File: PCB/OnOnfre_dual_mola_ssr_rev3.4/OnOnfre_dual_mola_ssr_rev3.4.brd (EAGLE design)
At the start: 44.4 x 47.7 mm, 24 parts, among them J3Y S8050, J7 8p, K1 OMRON-G3MB-202P-SSR2, K2 OMRON-G3MB-202P-SSR2, U2 esp12

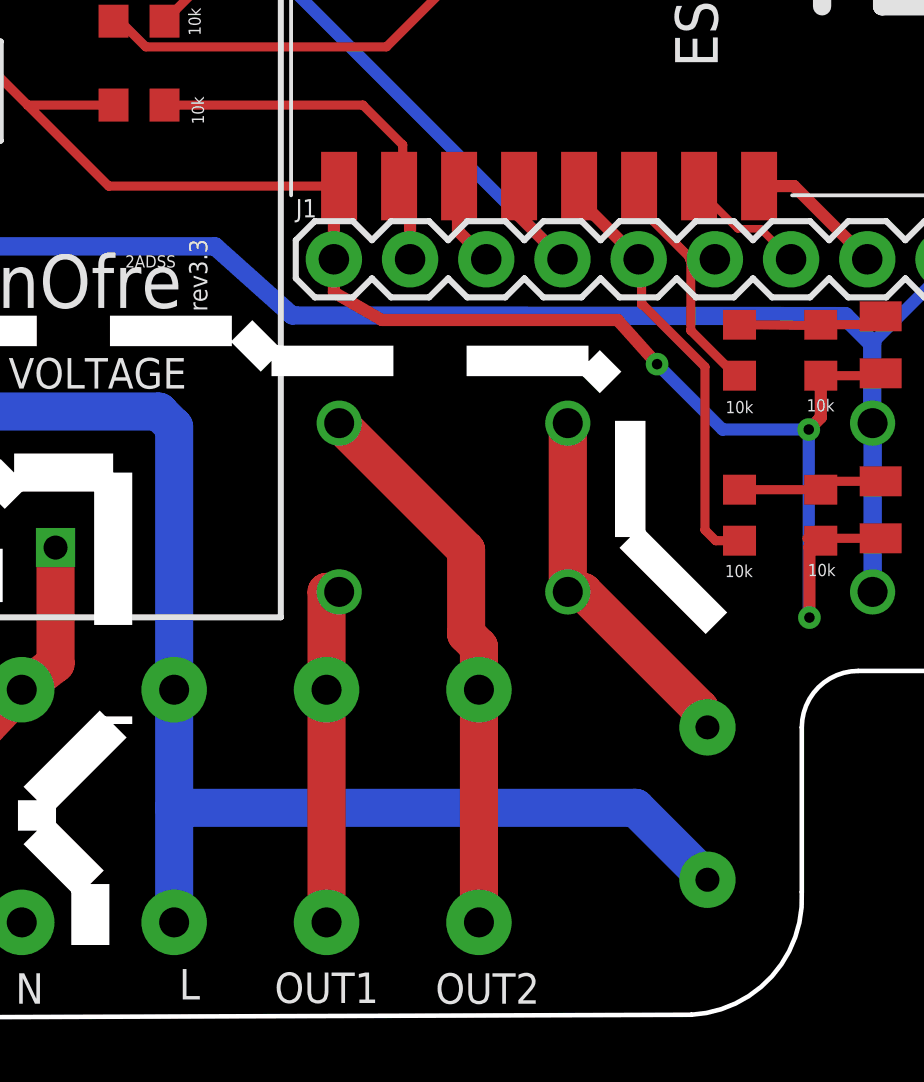
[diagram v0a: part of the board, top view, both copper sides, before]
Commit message: Rev 3.4, alteração de labels e numero de pinos
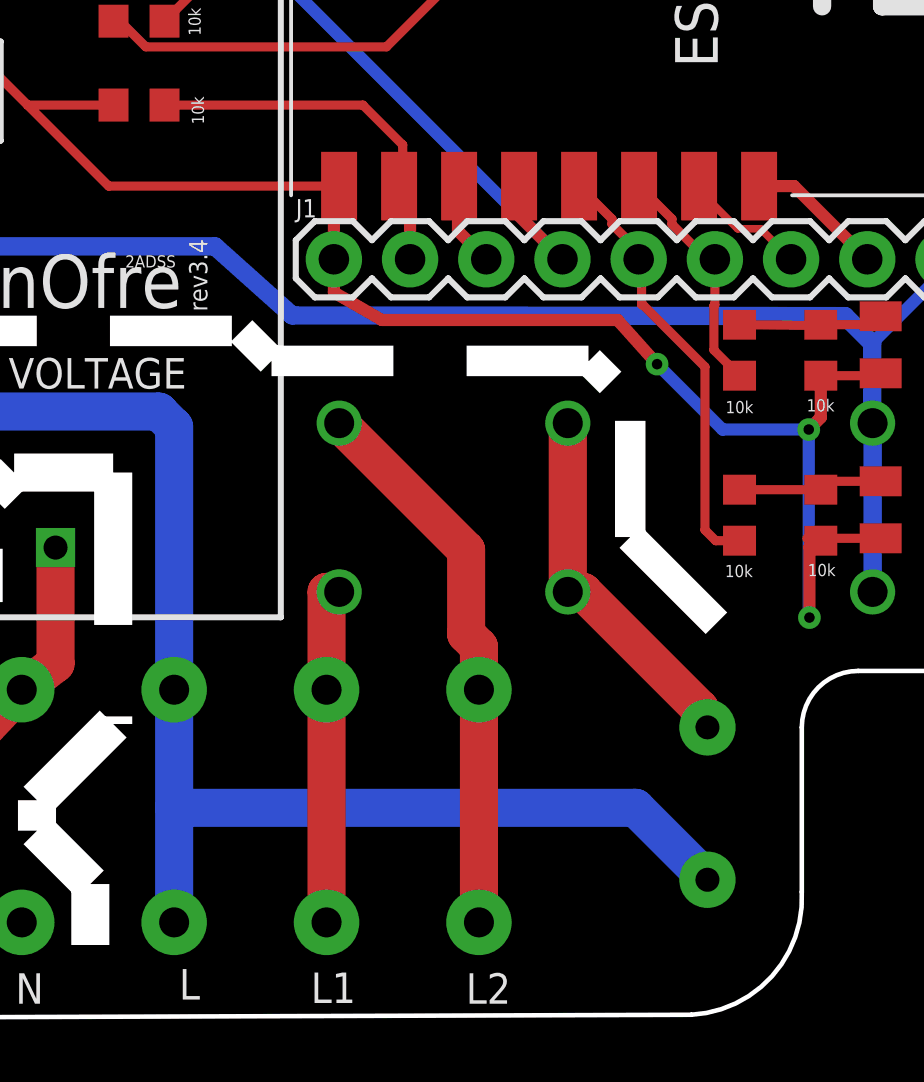
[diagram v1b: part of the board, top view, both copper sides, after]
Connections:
- net GPIO04: now also J1.5, R4.1; no longer J1.6, R1.1
- net GPIO05: now also J1.6, R1.1; no longer J1.5, R4.1
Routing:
- net GPIO05: track 14.6 -> 7.89 mm
- net GPIO04: track 8.65 -> 14.7 mm
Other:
- board text added: "L1"
- board text added: "L2"
- board text added: "rev3.4"
- board text removed: "OUT1"
- board text removed: "OUT2"
- board text removed: "rev3.3"
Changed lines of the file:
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@@
 <text x="27.8430875" y="27.2" size="1.016" layer="26" font="vector" ratio="13" rot="SMR270">02</text>
 <text x="30.39693125" y="27.2" size="1.016" layer="26" font="vector" ratio="13" rot="SMR270">00</text>
-<text x="35.008521875" y="26.946" size="1.016" layer="26" font="vector" ratio="13" rot="SMR270">05</text>
-<text x="32.933725" y="26.946" size="1.016" layer="26" font="vector" ratio="13" rot="SMR270">04</text>
+<text x="35.516521875" y="27.2" size="1.016" layer="26" font="vector" ratio="13" rot="SMR270">05</text>
+<text x="33.187725" y="27.2" size="1.016" layer="26" font="vector" ratio="13" rot="SMR270">04</text>
 <text x="37.976659375" y="27.2" size="1.016" layer="26" font="vector" ratio="13" rot="SMR270">RX</text>
 <text x="40.5769125" y="27.2" size="1.016" layer="26" font="vector" ratio="13" rot="SMR270">TX</text>
@@
 <text x="17.1611875" y="44.59194375" size="1.016" layer="25" font="vector" ratio="13">GND</text>
 <text x="2.07551875" y="19.564846875" size="1.016" layer="25" font="vector" ratio="13">DANGER HIGH VOLTAGE</text>
-<text x="25.727640625" y="-0.941734375" size="1.016" layer="25" font="vector" ratio="13">OUT2</text>
+<text x="26.743640625" y="-0.941734375" size="1.016" layer="25" font="vector" ratio="13">L2</text>
 <text x="17.182096875" y="-0.801503125" size="1.016" layer="25" font="vector" ratio="13">L</text>
 <text x="11.7294125" y="-0.941734375" size="1.016" layer="25" font="vector" ratio="13">N</text>
-<text x="34.81028125" y="28" size="0.6096" layer="26" font="vector" ratio="13" rot="MR135">OUT1</text>
-<text x="32.370396875" y="28" size="0.6096" layer="26" font="vector" ratio="13" rot="MR135">OUT2</text>
+<text x="32.52428125" y="28" size="0.6096" layer="26" font="vector" ratio="13" rot="MR135">L1</text>
+<text x="34.656396875" y="28" size="0.6096" layer="26" font="vector" ratio="13" rot="MR135">L2</text>
 <text x="10.06588125" y="18.99509375" size="1.6764" layer="25" font="vector" ratio="13" rot="R180">2A MAX</text>
 <text x="7.531659375" y="16.5151875" size="1.6764" layer="25" font="vector" ratio="13" rot="R180">230V</text>
-<text x="23.833728125" y="0.098490625" size="1.016" layer="25" font="vector" ratio="13" rot="R180">OUT1</text>
+<text x="23.071728125" y="0.098490625" size="1.016" layer="25" font="vector" ratio="13" rot="R180">L1</text>
 <wire x1="0.408834375" y1="12.034521875" x2="0.408834375" y2="11.952653125" width="0.1524" layer="20"/>
 <wire x1="0.408834375" y1="11.952653125" x2="0.408834375" y2="8.747953125" width="0.1524" layer="20"/>
@@
 <wire x1="32.2216125" y1="18.487096875" x2="32.2216125" y2="14.613959375" width="1.016" layer="46" style="shortdash"/>
 <wire x1="32.2216125" y1="14.613959375" x2="36.81131875" y2="10.024253125" width="1.016" layer="46" style="shortdash"/>
-<text x="18.12618125" y="22.133634375" size="0.6096" layer="25" rot="R90">rev3.3</text>
+<text x="18.12618125" y="22.133634375" size="0.6096" layer="25" rot="R90">rev3.4</text>
 <text x="15.387978125" y="23.598921875" size="0.4064" layer="25">2ADSS</text>
 <wire x1="0.508" y1="11.938" x2="20.574" y2="11.938" width="0.2" layer="25"/>
@@
 <signal name="GPIO04">
 <contactref element="U2" pad="GPIO4"/>
-<contactref element="R1" pad="1"/>
-<wire x1="32.4965375" y1="26.164065625" x2="32.434640625" y2="25.700809375" width="0.3048" layer="1"/>
-<wire x1="34.239946875" y1="23.895503125" x2="32.434640625" y2="25.700809375" width="0.3048" layer="1"/>
-<wire x1="35.864153125" y1="19.992975" x2="35.775996875" y2="19.96474375" width="0.3048" layer="1"/>
-<wire x1="35.775996875" y1="19.96474375" x2="34.239946875" y2="21.50079375" width="0.3048" layer="1"/>
-<wire x1="34.239946875" y1="21.50079375" x2="34.239946875" y2="23.895503125" width="0.3048" layer="1"/>
-<contactref element="J1" pad="6"/>
-<wire x1="32.516375" y1="26.31254375" x2="32.516375" y2="26.183903125" width="0.4064" layer="1"/>
-<wire x1="32.516375" y1="26.183903125" x2="32.4965375" y2="26.164065625" width="0.4064" layer="1"/>
-<wire x1="35.042321875" y1="23.872990625" x2="34.262459375" y2="23.872990625" width="0.4064" layer="1"/>
-<wire x1="34.262459375" y1="23.872990625" x2="34.239946875" y2="23.895503125" width="0.4064" layer="1"/>
-</signal>
-<signal name="GPIO05">
-<contactref element="U2" pad="GPIO5"/>
+<contactref element="J1" pad="5"/>
 <contactref element="R4" pad="1"/>
-<wire x1="30.434640625" y1="25.940671875" x2="30.516375" y2="26.31254375" width="0.3048" layer="1"/>
 <wire x1="35.864153125" y1="14.4911875" x2="35.071171875" y2="14.4911875" width="0.3048" layer="1"/>
 <wire x1="35.071171875" y1="14.4911875" x2="34.711759375" y2="14.8506" width="0.3048" layer="1"/>
 <wire x1="34.711759375" y1="14.8506" x2="34.711759375" y2="20.28758125" width="0.3048" layer="1"/>
-<wire x1="32.64480625" y1="22.354534375" x2="32.59984375" y2="22.354534375" width="0.3048" layer="1"/>
-<wire x1="32.59984375" y1="23.77546875" x2="32.59984375" y2="22.354534375" width="0.3048" layer="1"/>
+<wire x1="32.59984375" y1="22.354534375" x2="32.64480625" y2="22.354534375" width="0.3048" layer="1"/>
 <wire x1="34.711759375" y1="20.28758125" x2="32.64480625" y2="22.354534375" width="0.3048" layer="1"/>
-<contactref element="J1" pad="5"/>
-<wire x1="32.502321875" y1="23.872990625" x2="30.434640625" y2="25.940671875" width="0.4064" layer="1"/>
-<wire x1="32.502321875" y1="23.872990625" x2="32.59984375" y2="23.77546875" width="0.4064" layer="1"/>
+<wire x1="30.516375" y1="26.31254375" x2="31.611575" y2="25.21734375" width="0.3048" layer="1"/>
+<wire x1="31.611575" y1="25.21734375" x2="31.611575" y2="25.04329375" width="0.3048" layer="1"/>
+<wire x1="31.611575" y1="25.04329375" x2="32.59984375" y2="24.055025" width="0.3048" layer="1"/>
+<wire x1="32.59984375" y1="24.055025" x2="32.59984375" y2="23.77546875" width="0.3048" layer="1"/>
+<wire x1="32.59984375" y1="23.622" x2="32.59984375" y2="22.354534375" width="0.3048" layer="1"/>
+<wire x1="32.502321875" y1="23.872990625" x2="32.59984375" y2="23.77546875" width="0.3048" layer="1"/>
+<wire x1="32.59984375" y1="23.77546875" x2="32.59984375" y2="23.622" width="0.3048" layer="1"/>
+</signal>
+<signal name="GPIO05">
+<contactref element="U2" pad="GPIO5"/>
+<contactref element="J1" pad="6"/>
+<contactref element="R1" pad="1"/>
+<wire x1="32.516375" y1="26.31254375" x2="33.611575" y2="25.21734375" width="0.3048" layer="1"/>
+<wire x1="33.611575" y1="25.21734375" x2="33.611575" y2="25.04329375" width="0.3048" layer="1"/>
+<wire x1="33.611575" y1="25.04329375" x2="34.781878125" y2="23.872990625" width="0.3048" layer="1"/>
+<wire x1="34.781878125" y1="23.872990625" x2="35.042321875" y2="23.872990625" width="0.3048" layer="1"/>
+<wire x1="35.042321875" y1="23.872990625" x2="35.042321875" y2="22.352190625" width="0.3048" layer="1"/>
+<wire x1="35.042321875" y1="22.352190625" x2="35.009353125" y2="22.319221875" width="0.3048" layer="1"/>
+<wire x1="35.009353125" y1="22.319221875" x2="35.009353125" y2="20.847775" width="0.3048" layer="1"/>
+<wire x1="35.009353125" y1="20.847775" x2="35.864153125" y2="19.992975" width="0.3048" layer="1"/>
 </signal>
 <signal name="GPIO02">
